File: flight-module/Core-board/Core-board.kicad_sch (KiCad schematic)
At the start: 16 parts, among them J1 Stack_Shape, J4 Conn_01x06_Pin, U7 XTSD04GLGEAG, U8 74HC4050D

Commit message: Finished flight-core.
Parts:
- removed R1, R2, R3, R7, R8, R9: 100kΩ, Resistor_SMD:R_0603_1608Metric, symbol Device:R_Small
- removed R10, R11, R12, R4, R5, R6: 2kΩ, Resistor_SMD:R_0603_1608Metric, symbol Device:R_Small
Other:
- moved on the sheet: J4

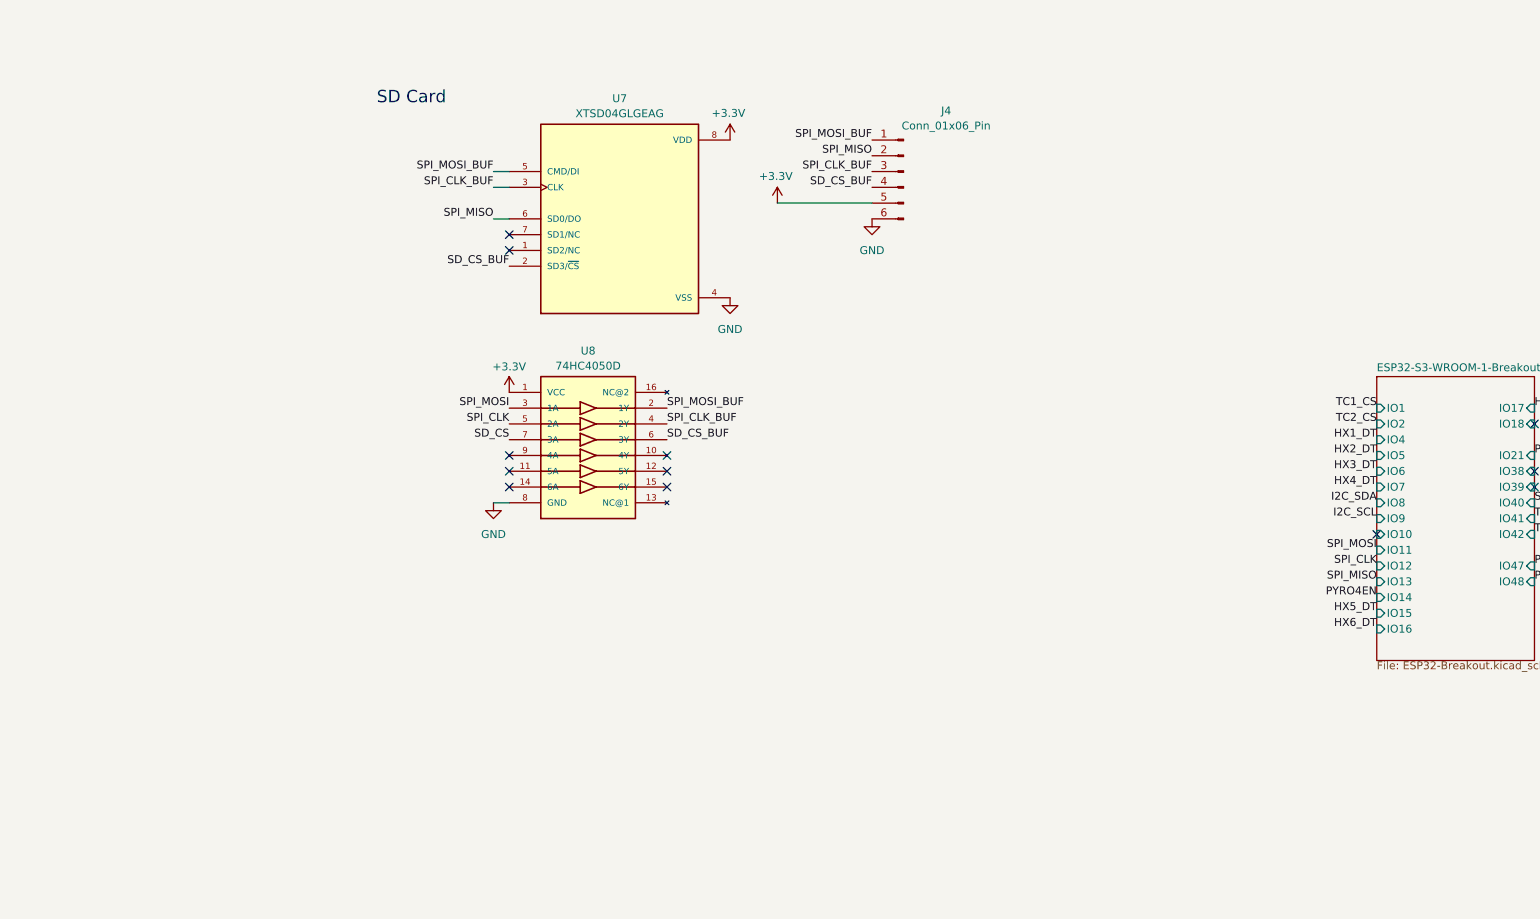
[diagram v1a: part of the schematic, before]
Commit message: Minor changes to footprint library
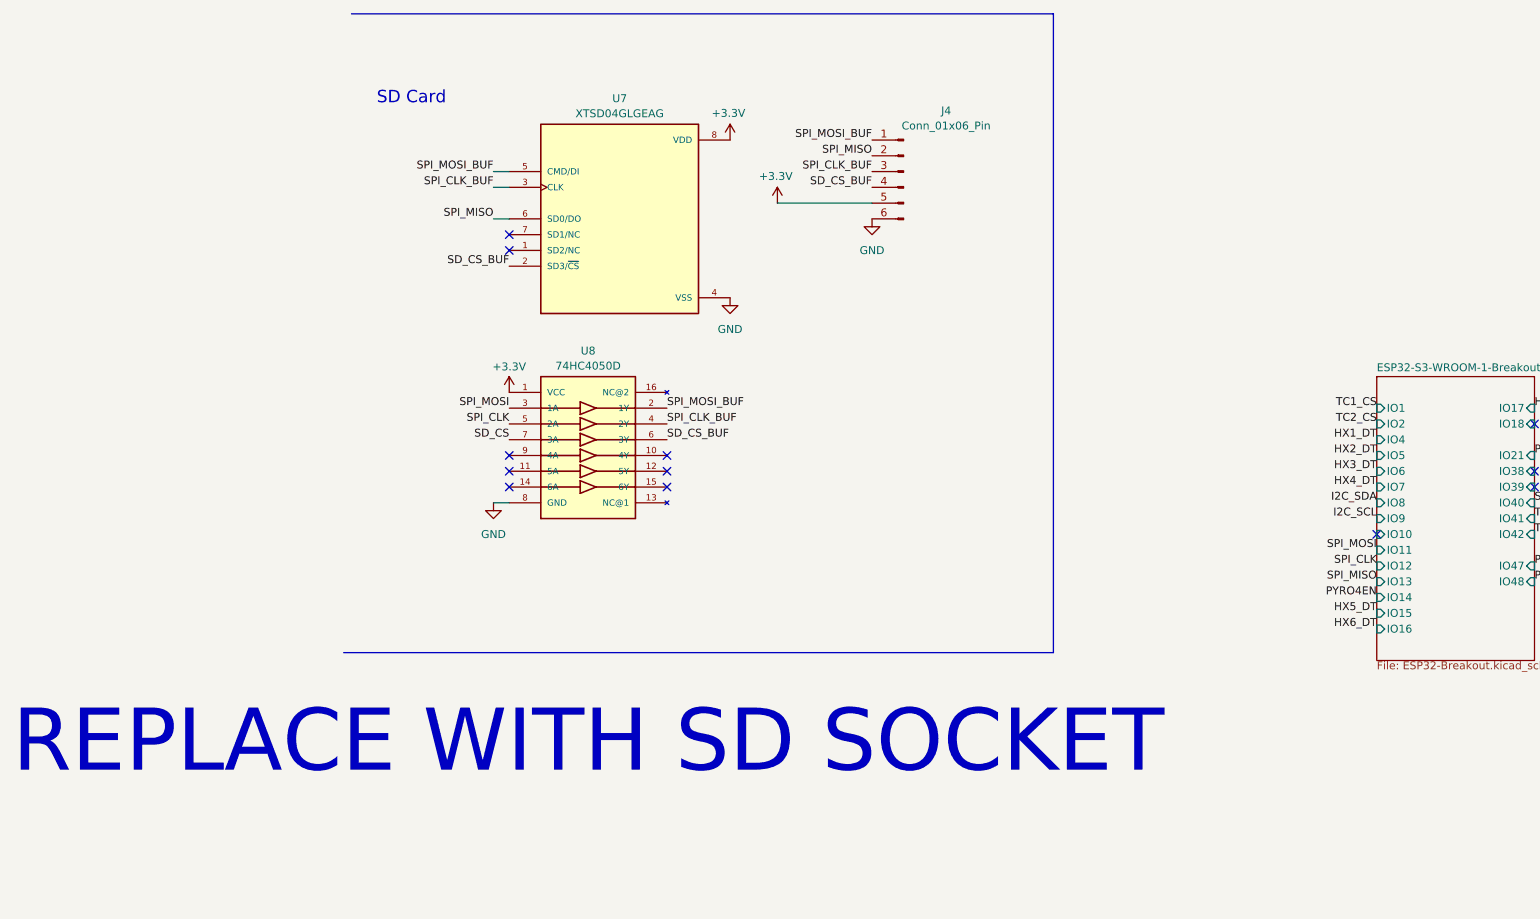
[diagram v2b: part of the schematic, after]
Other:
- note added: "REPLACE WITH SD SOCKET"
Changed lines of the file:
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@@
+    (stroke (width 0) (type default))
+  )
+  (bus (pts (xy 27.94 30.48) (xy 140.97 30.48))
     (stroke (width 0) (type default))
   )
@@
     (stroke (width 0) (type default))
   )
+  (bus (pts (xy 26.67 133.35) (xy 140.97 133.35))
+    (stroke (width 0) (type default))
+  )
   (wire (pts (xy 48.26 213.36) (xy 48.26 220.98))
     (stroke (width 0) (type default))
@@
     (stroke (width 0) (type default))
   )
+  (bus (pts (xy 140.97 30.48) (xy 140.97 133.35))
+    (stroke (width 0) (type default))
+  )
   (wire (pts (xy 383.54 86.36) (xy 388.62 86.36))
     (stroke (width 0) (type default))
@@
     (stroke (width 0) (type default))
   )
+  (text "REPLACE WITH SD SOCKET" (at -26.67 153.67 0)
+    (effects (font (size 10 10)) (justify left bottom))
+  )
   (text "SD Card" (at 32.004 45.212 0)

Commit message: core board sd card and HX2 HX6 changes
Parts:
- removed J4: Conn_01x06_Pin, Connector_PinHeader_2.54mm:PinHeader_1x06_P2.54mm_Vertical, symbol Connector:Conn_01x06_Pin
- removed U7: XTSD04GLGEAG, XTSD04GLGEAG:SON127P600X800X95-8N, symbol XTSD_NAND:XTSD04GLGEAG
- removed U8: 74HC4050D, 74HC4050D:SO16, symbol Buf_74HC4050D:74HC4050D
- added J10: Conn_01x07_Pin, Connector_PinSocket_2.54mm:PinSocket_1x07_P2.54mm_Vertical, symbol Connector:Conn_01x07_Pin
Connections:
- net +3.3V: now also J10.2 (Pin_2)
- net GND: now also J10.3 (Pin_3)
- net SD_CS: now also J10.7 (Pin_7)
- net SPI_CLK: now also J10.4 (Pin_4)
- net SPI_MISO: now also J10.5 (Pin_5)
- net SPI_MOSI: now also J10.6 (Pin_6)
- no-connect marks 34 -> 27
